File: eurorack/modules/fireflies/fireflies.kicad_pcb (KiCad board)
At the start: 2 copper layers, 37 parts, among them J1 Conn_02x05_Odd_Even, U1 4051, U2 4051, U3 ProMicro, U4 TLC5971PWP

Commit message: start rethinking fireflies around chordata
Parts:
- removed the C1 at (144.4, 97.9)
- removed the C2 at (142.3, 109.4)
- removed the R13 at (136.3, 121.5)
- removed the R14 at (161.8, 98.9)
- removed the R6 at (131.5, 124.5)
- added C10: 100n, Capacitor_SMD:C_0805_2012Metric_Pad1.18x1.45mm_HandSolder, B.Cu at (75.8, 50.9)
- added C12: 1u, Capacitor_SMD:C_0805_2012Metric_Pad1.18x1.45mm_HandSolder, B.Cu at (55.4, 49.0)
- added C4: 10u, Capacitor_SMD:C_0805_2012Metric_Pad1.18x1.45mm_HandSolder, B.Cu at (70.0, 118.2)
- added C5: 10u, Capacitor_SMD:C_0805_2012Metric_Pad1.18x1.45mm_HandSolder, B.Cu at (63.9, 118.2)
- added C7: 100n, Capacitor_SMD:C_0805_2012Metric_Pad1.18x1.45mm_HandSolder, B.Cu at (58.0, 118.2)
- added J2: AudioJack2_SwitchT, Pale Slim Ghost:Jack_3.5mm_QingPu_WQP-PJ398SM_Vertical, F.Cu at (56.4, 127.8)
- added J3: AudioJack2_SwitchT, Pale Slim Ghost:Jack_3.5mm_QingPu_WQP-PJ398SM_Vertical, F.Cu at (65.5, 127.8)
- added J4: AudioJack2_SwitchT, Pale Slim Ghost:Jack_3.5mm_QingPu_WQP-PJ398SM_Vertical, F.Cu at (66.0, 140.7)
- added J5: AudioJack2_SwitchT, Pale Slim Ghost:Jack_3.5mm_QingPu_WQP-PJ398SM_Vertical, F.Cu at (55.9, 140.7)
- added R4: 10k, Resistor_SMD:R_0805_2012Metric_Pad1.20x1.40mm_HandSolder, B.Cu at (62.7, 124.6)
- added R8: 220, Resistor_SMD:R_0805_2012Metric_Pad1.20x1.40mm_HandSolder, B.Cu at (62.5, 138.0)
- added REF**: RotaryEncoder_Alps_EC11E-Switch_Vertical_H20mm, Rotary_Encoder:RotaryEncoder_Alps_EC11E-Switch_Vertical_H20mm, F.Cu at (35.9, 82.5)
- added SW1: SW_Push_LED, Pale Slim Ghost:PB01-109TL, F.Cu at (56.1, 112.9)
- added SW2: SW_Push_LED, Pale Slim Ghost:PB01-109TL, F.Cu at (65.8, 112.9)
- C1: renamed from C3; moved to B.Cu
- C11: renamed from C9; moved to B.Cu
- C13: renamed from C10; moved to B.Cu
- C2: renamed from C4; moved to B.Cu
- C3: renamed from C5; moved to B.Cu
- C6, U4: moved to B.Cu
- C8: renamed from C7; moved to B.Cu
- C9: renamed from C8; moved to B.Cu
- D1, D2: value D -> D_Zener; footprint Diode_SMD:D_SOD-123 -> Diode_SMD:D_0805_2012Metric_Pad1.15x1.40mm_HandSolder; moved to B.Cu
- J1: value Conn_02x05_Odd_Even -> Conn_01x04; footprint Connector_PinHeader_2.54mm:PinHeader_2x05_P2.54mm_Vertical_SMD -> Pale Slim Ghost:Stemma QT Qwiic JST_SH_SM04B; moved to B.Cu
- R1, R15, R7: value R -> 4k7; moved to B.Cu
- R10, R2: value R -> 1k; moved to B.Cu
- R11, R5: value R -> 560; moved to B.Cu
- R12: renamed from R8; value R -> 4k7; moved to B.Cu
- R13: renamed from R12; value R -> 4k7; moved to B.Cu
- R14: renamed from R16; value R -> 4k7; moved to B.Cu
- R3: value R -> 10k; moved to B.Cu
- R6: renamed from R4; value R -> 4k7; moved to B.Cu
- R9: value R -> 220; moved to B.Cu
- S1, S2, S3, S4: footprint Switches:ENCODER_LED_3 -> Pale Slim Ghost:ENCODER_LED_3
- U1: value 4051 -> MIC5219-5.0YM5; footprint Package_SO:TSSOP-16_4.4x5mm_P0.65mm -> Package_TO_SOT_SMD:SOT-23-5; moved to B.Cu
- U2: value 4051 -> Chordata; footprint Package_SO:TSSOP-16_4.4x5mm_P0.65mm -> Pale Slim Ghost:Chordata; moved to B.Cu
- U3: value ProMicro -> MCP4822; footprint promicro:ProMicro-NoSilk -> Package_SO:MSOP-8_3x3mm_P0.65mm; moved to B.Cu
- moved S2 150.5 mm to (62.4, 58.5), turned to 90 degrees
- moved S1 144.0 mm to (59.1, 45.2), turned to 90 degrees
- moved S3 120.7 mm to (59.1, 71.9), turned to 90 degrees
- moved S4 118.7 mm to (62.4, 85.2), turned to 90 degrees
- moved R15 115.7 mm to (56.5, 43.1), turned to -90 degrees
- moved R6 104.9 mm to (67.3, 40.3), turned to -90 degrees
- moved R1 102.3 mm to (61.0, 113.0), turned to -90 degrees
- moved R12 99.2 mm to (60.7, 60.6), turned to 90 degrees
- moved R5 98.6 mm to (58.8, 107.3), turned to -90 degrees
- moved D1 98.0 mm to (59.2, 128.4), turned to -90 degrees
- moved R9 96.9 mm to (59.4, 138.0), turned to 90 degrees
- moved R10 92.8 mm to (63.1, 107.3), turned to -90 degrees
- moved C1 92.4 mm to (72.0, 50.9)
- moved C11 92.4 mm to (65.3, 85.5), turned to 90 degrees
- moved C6 91.2 mm to (65.4, 71.6), turned to 90 degrees
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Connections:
- D1 pad 1: +12V -> Input 1
- D1 pad 2: Net-(D1-Pad2) -> GND
- D2 pad 1: +12V -> Input 2
- D2 pad 2: Net-(D2-Pad2) -> GND
- J1 pad 1: Net-(D1-Pad2) -> SCL
- J1 pad 2: Net-(D1-Pad2) -> SDA
- J1 pad 3: GND -> unconnected-(J1-Pad3)
- R1 pad 2: LED 1 R -> GND
- R10 pad 1: Net-(R10-Pad1) -> Switch 2
- R10 pad 2: LED 3 G -> Net-(R10-Pad2)
- R11 pad 2: LED 3 B -> Switch LED 2
- R12 pad 2: switch 2 -> encoder 2 switch
- R13 pad 2: switch 3 -> encoder 3 switch
- R14 pad 2: switch 4 -> encoder 4 switch
- R15 pad 1: Net-(R15-Pad1) -> GND
- R15 pad 2: LED 4 B -> Net-(R15-Pad2)
- R2 pad 1: Net-(R2-Pad1) -> Switch 1
- R2 pad 2: LED 1 G -> Net-(R1-Pad1)
- R3 pad 1: Net-(R3-Pad1) -> Net-(J2-PadT)
- R3 pad 2: LED 1 B -> Input 1
- R5 pad 2: LED 2 R -> Switch LED 1
- R6 pad 2: switch 1 -> encoder 1 switch
- R7 pad 1: Net-(R7-Pad1) -> Net-(R10-Pad2)
- R7 pad 2: LED 2 B -> GND
- R9 pad 1: Net-(R9-Pad1) -> Net-(J5-PadT)
- R9 pad 2: LED 3 R -> Output 2
- S1 pad 1: Net-(R1-Pad1) -> LED 1 R
- S1 pad 2: Net-(R2-Pad1) -> LED 1 G
- S1 pad 3: switch 1 -> encoder 1 switch
- S1 pad 4: Net-(R3-Pad1) -> LED 1 B
- S2 pad 1: Net-(R5-Pad1) -> LED 2 R
- S2 pad 2: Net-(R6-Pad1) -> LED 2 G
- S2 pad 3: switch 2 -> encoder 2 switch
- S2 pad 4: Net-(R7-Pad1) -> LED 2 B
- S3 pad 1: Net-(R9-Pad1) -> LED 3 R
- S3 pad 2: Net-(R10-Pad1) -> LED 3 G
- S3 pad 3: switch 3 -> encoder 3 switch
- S3 pad 4: Net-(R11-Pad1) -> LED 3 B
- S4 pad 1: Net-(R13-Pad1) -> LED 4 R
- S4 pad 2: Net-(R14-Pad1) -> LED 4 G
- S4 pad 3: switch 4 -> encoder 4 switch
- S4 pad 4: Net-(R15-Pad1) -> LED 4 B
- U1 pad 1: encoder 3 A -> +12V
- U1 pad 2: encoder 4 A -> GND
- U1 pad 3: Mux 1 -> +12V
- U1 pad 4: encoder 4 B -> unconnected-(U1-Pad4)
- U1 pad 5: encoder 3 B -> +5V
- U2 pad 1: unconnected-(U2-Pad1) -> encoder 1 A
- U2 pad 10: Mux B -> Switch LED 1
- U2 pad 11: Mux A -> Switch 2
- U2 pad 12: unconnected-(U2-Pad12) -> Switch LED 2
- U2 pad 15: unconnected-(U2-Pad15) -> SCK2
- U2 pad 16: unconnected-(U2-Pad16) -> COPI2
- U2 pad 2: unconnected-(U2-Pad2) -> encoder 2 switch
- U2 pad 3: Mux 2 -> encoder 2 A
- U2 pad 4: unconnected-(U2-Pad4) -> encoder 3 B
- U2 pad 5: unconnected-(U2-Pad5) -> encoder 3 switch
- U2 pad 6: unconnected-(U2-Pad6) -> encoder 4 B
- U2 pad 7: unconnected-(U2-Pad7) -> encoder 4 switch
- U2 pad 9: Mux C -> Switch 1
- U3 pad 1: unconnected-(U3-Pad1) -> +5V
- U3 pad 2: unconnected-(U3-Pad2) -> CS1
- U3 pad 3: GND -> SCK1
- U3 pad 4: GND -> COPI1
- U3 pad 6: unconnected-(U3-Pad6) -> Output 2
- U3 pad 7: unconnected-(U3-Pad7) -> GND
- U3 pad 8: unconnected-(U3-Pad8) -> Output 1
- U4 pad 1: unconnected-(U4-Pad1) -> Net-(R15-Pad2)
- U4 pad 10: unconnected-(U4-Pad10) -> SCK2
- U4 pad 19: unconnected-(U4-Pad19) -> +12V
- U4 pad 2: Net-(U4-Pad2) -> GND
- U4 pad 20: unconnected-(U4-Pad20) -> Net-(C12-Pad1)
- U4 pad 21: Net-(U4-Pad2) -> GND
- U4 pad 9: unconnected-(U4-Pad9) -> COPI2
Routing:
- added copper zone on F.Cu, net +3V3
- added copper zone on B.Cu, net GND
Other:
- board outline added: 20.3 x 109.2 mm

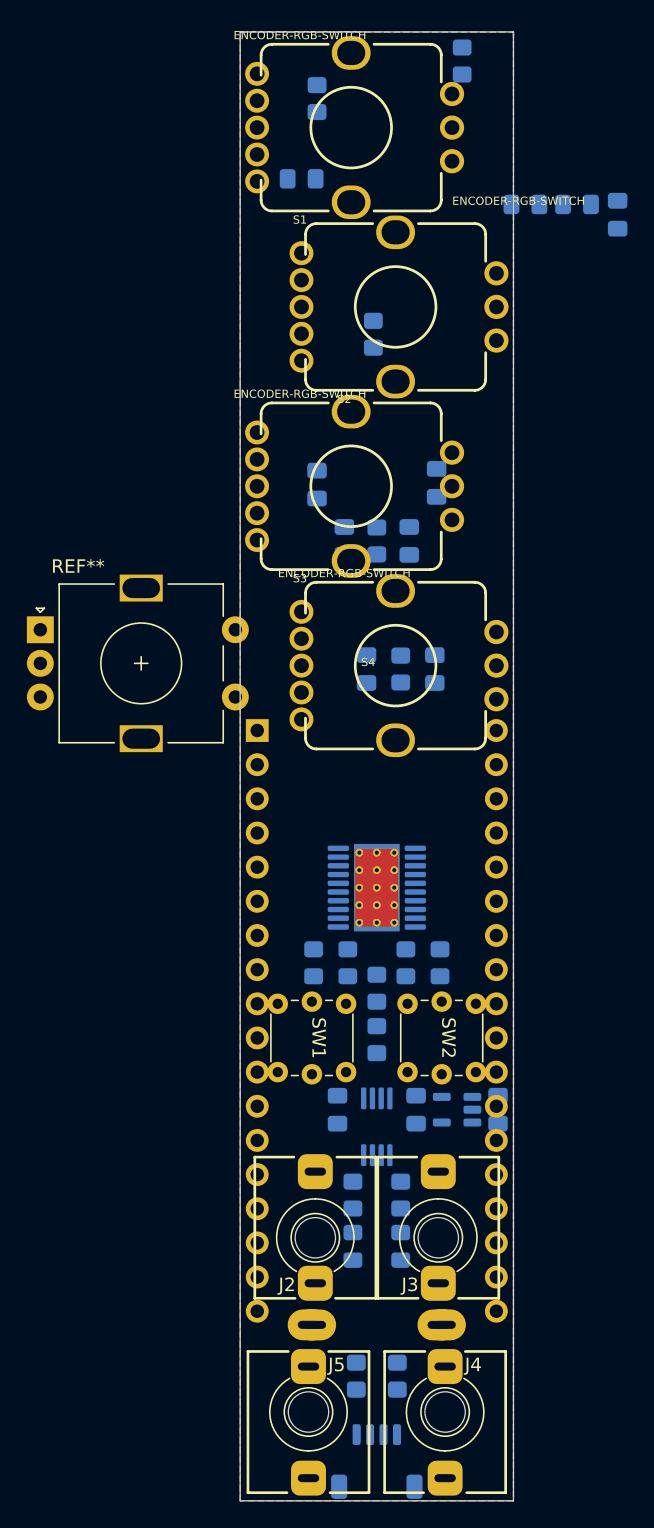
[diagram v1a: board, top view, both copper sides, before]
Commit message: wip fireflies redesign
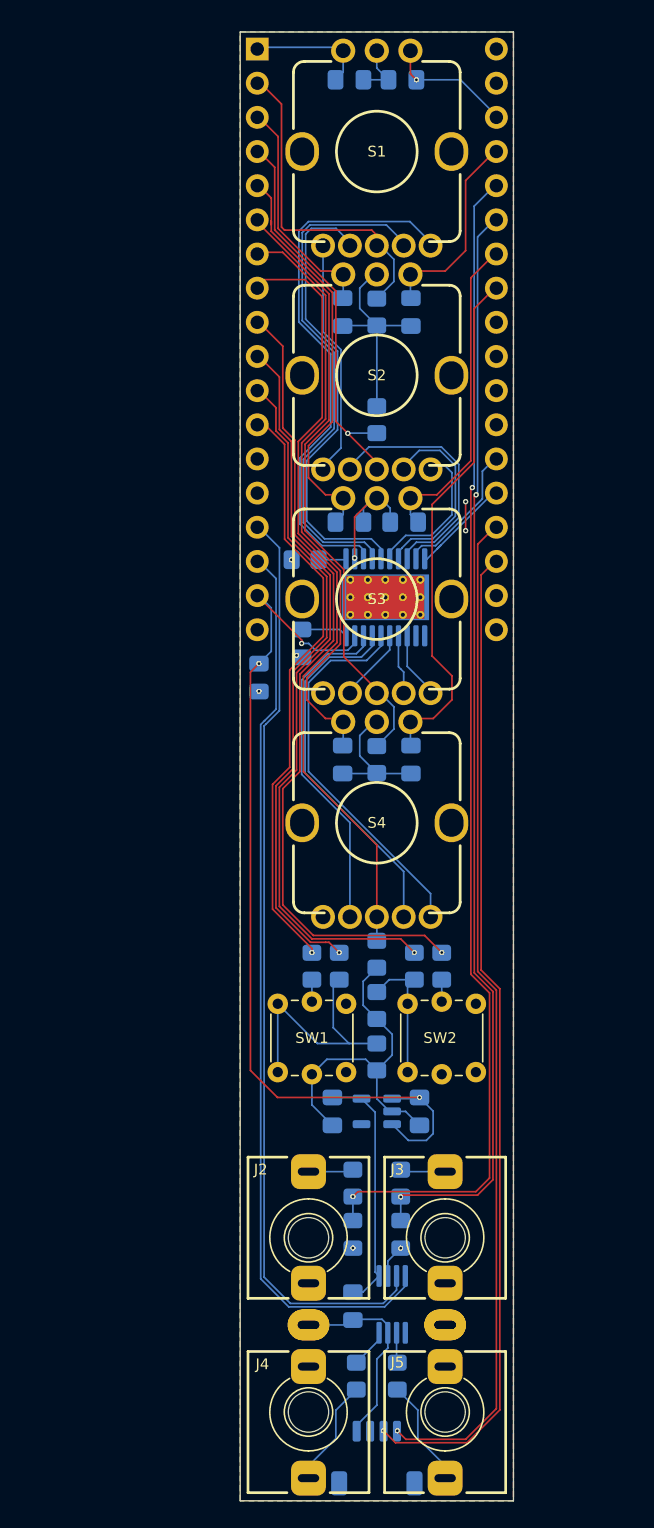
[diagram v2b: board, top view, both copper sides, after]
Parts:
- removed REF**: RotaryEncoder_Alps_EC11E-Switch_Vertical_H20mm, Rotary_Encoder:RotaryEncoder_Alps_EC11E-Switch_Vertical_H20mm
- moved U2 50.7 mm to (61.0, 61.0)
- moved C10 42.4 mm to (52.2, 86.1), turned to 90 degrees
- moved C12 34.5 mm to (55.4, 83.6), turned to -90 degrees
- moved R15 34.3 mm to (55.6, 77.3), turned to 0 degrees
- moved C2 22.3 mm to (58.9, 41.7), turned to 0 degrees
- moved U4 21.6 mm to (61.6, 80.1), turned to -90 degrees
- moved R14 21.3 mm to (61.0, 106.7), turned to 90 degrees
- moved R6 19.7 mm to (61.0, 58.9), turned to 90 degrees
- moved R13 16.3 mm to (61.0, 92.2), turned to 90 degrees
- moved C7 14.6 mm to (59.2, 132.8), turned to 90 degrees
- moved C3 14.6 mm to (63.5, 58.9)
- moved C6 14.5 mm to (58.4, 58.9), turned to -90 degrees
- moved U3 13.3 mm to (62.1, 132.7)
- moved C1 13.0 mm to (62.9, 41.7)
- moved S4 11.8 mm to (61.0, 96.9), turned to 180 degrees
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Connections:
- U2 pad 1: encoder 1 A -> encoder 1 B
- U2 pad 10: Switch LED 1 -> Switch 2
- U2 pad 11: Switch 2 -> Switch 1
- U2 pad 12: Switch LED 2 -> Switch LED 1
- U2 pad 14: unconnected-(U2-Pad14) -> CS1
- U2 pad 15: SCK2 -> SCK1
- U2 pad 16: COPI2 -> COPI1
- U2 pad 2: encoder 2 switch -> encoder 1 switch
- U2 pad 21: CS1 -> SDA
- U2 pad 22: unconnected-(U2-Pad22) -> SCL
- U2 pad 23: SCK1 -> SCK2
- U2 pad 24: COPI1 -> COPI2
- U2 pad 25: SDA -> unconnected-(U2-Pad25)
- U2 pad 26: SCL -> unconnected-(U2-Pad26)
- U2 pad 28: encoder 4 A -> unconnected-(U2-Pad28)
- U2 pad 29: encoder 3 A -> encoder 4 A
- U2 pad 3: encoder 2 A -> encoder 2 B
- U2 pad 30: encoder 2 B -> encoder 3 A
- U2 pad 31: encoder 1 B -> Input 2
- U2 pad 32: Input 2 -> Input 1
- U2 pad 33: Input 1 -> encoder 2 A
- U2 pad 34: encoder 1 switch -> encoder 1 A
- U2 pad 4: encoder 3 B -> encoder 2 switch
- U2 pad 5: encoder 3 switch -> encoder 3 B
- U2 pad 6: encoder 4 B -> encoder 3 switch
- U2 pad 7: encoder 4 switch -> encoder 4 B
- U2 pad 8: unconnected-(U2-Pad8) -> encoder 4 switch
- U2 pad 9: Switch 1 -> Switch LED 2
- U3 pad 2: CS1 -> GND
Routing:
- net Input 1: track 0.00 -> 87.8 mm, vias 0 -> 2
- net GND: track 0.00 -> 85.3 mm, vias 0 -> 6
- net Input 2: track 0.00 -> 82.0 mm, vias 0 -> 2
- net SCL: track 0.00 -> 75.4 mm, vias 0 -> 1
- net SDA: track 0.00 -> 74.3 mm, vias 0 -> 1
- net SCK1: track 0.00 -> 69.2 mm
- net +12V: track 0.00 -> 68.7 mm, vias 0 -> 3
- net COPI1: track 0.00 -> 67.5 mm
- net Switch LED 2: track 0.00 -> 60.6 mm, vias 0 -> 1
- net encoder 4 switch: track 0.00 -> 58.7 mm
- net Switch 2: track 0.00 -> 56.3 mm, vias 0 -> 1
- net Switch 1: track 0.00 -> 48.4 mm, vias 0 -> 1
- net encoder 3 switch: track 0.00 -> 45.5 mm
- net encoder 4 B: track 0.00 -> 44.8 mm
- net Switch LED 1: track 0.00 -> 44.4 mm, vias 0 -> 1
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- added copper zone on B.Cu, net +3V3
- added copper zone on F.Cu, net GND
- removed copper zone on F.Cu, net +3V3
- removed copper zone on B.Cu, net GND

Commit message: i honestly have no idea
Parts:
- added R16: 10k, Resistor_SMD:R_0805_2012Metric_Pad1.20x1.40mm_HandSolder, B.Cu at (58.4, 131.3)
- added R17: 10k, Resistor_SMD:R_0805_2012Metric_Pad1.20x1.40mm_HandSolder, B.Cu at (58.4, 138.9)
- added R18: 10k, Resistor_SMD:R_0805_2012Metric_Pad1.20x1.40mm_HandSolder, B.Cu at (63.5, 131.3)
- added R19: 10k, Resistor_SMD:R_0805_2012Metric_Pad1.20x1.40mm_HandSolder, B.Cu at (63.5, 138.9)
- C4, C5: value 10u -> 100n
- U1: value MIC5219-5.0YM5 -> TL072; footprint Package_TO_SOT_SMD:SOT-23-5 -> Package_TO_SOT_SMD:SOT-23-8_Handsoldering
- moved C4 20.8 mm to (61.0, 138.9), turned to 90 degrees
- moved U1 16.8 mm to (61.0, 135.1), turned to 0 degrees
- moved C7 14.2 mm to (56.6, 118.9), turned to -90 degrees
- moved U3 14.1 mm to (61.0, 118.6), turned to 0 degrees
- moved C5 13.4 mm to (61.0, 131.3), turned to 90 degrees
- moved R8 8.71 mm to (53.3, 144.3)
- moved R9 8.71 mm to (68.6, 144.3)
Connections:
- C4 pad 1: +12V -> GND
- C4 pad 2: GND -> +12V
- C5 pad 1: +5V -> -12V
- C7 pad 2: +5V -> +3V3
- U1 pad 1: +12V -> Output 1
- U1 pad 2: GND -> Net-(R16-Pad2)
- U1 pad 3: +12V -> Output 1 raw
- U1 pad 4: unconnected-(U1-Pad4) -> -12V
- U1 pad 5: +5V -> Output 2 raw
- U3 pad 1: +5V -> +3V3
- U3 pad 6: Output 2 -> Output 2 raw
- U3 pad 8: Output 1 -> Output 1 raw
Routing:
- net -12V: track 0.00 -> 64.0 mm, vias 0 -> 2
- net COPI1: track 67.5 -> 48.3 mm
- net +5V: track 18.4 -> 0.00 mm
- net Output 1 raw: track 0.00 -> 18.3 mm
- net Output 2 raw: track 0.00 -> 18.0 mm
- net SCK1: track 69.2 -> 53.4 mm
- net Output 2: track 2.24 -> 13.0 mm
- net +12V: track 68.7 -> 78.0 mm
- net Output 1: track 2.92 -> 11.2 mm
- net Net-(R18-Pad2): track 0.00 -> 7.68 mm
- net Net-(R16-Pad2): track 0.00 -> 7.15 mm
- net Net-(J5-PadT): track 8.06 -> 2.69 mm
- net Net-(J4-PadT): track 8.06 -> 2.69 mm
- net GND: track 85.3 -> 80.7 mm, vias 6 -> 7
